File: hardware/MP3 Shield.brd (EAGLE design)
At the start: 53.3 x 59.7 mm, 62 parts, among them J1 ISP/SPI, Q1 12.288MHz, U1 3.3V, U2 ARDUINO_R3_SHIELD, U3 VS1053, U4 1.8V, U6 USD-SOCKET, U7 74HC4050 LVL CONVERTER

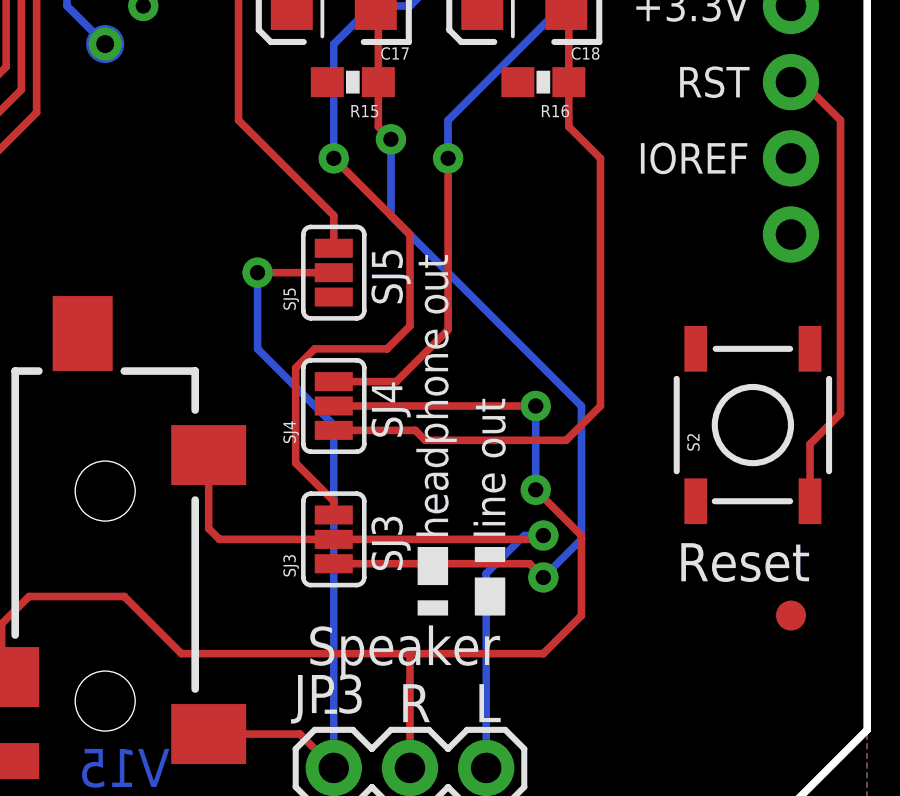
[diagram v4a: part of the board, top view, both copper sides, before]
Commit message: Tweaking after review
Clarifying solder jumpers for output configuration.
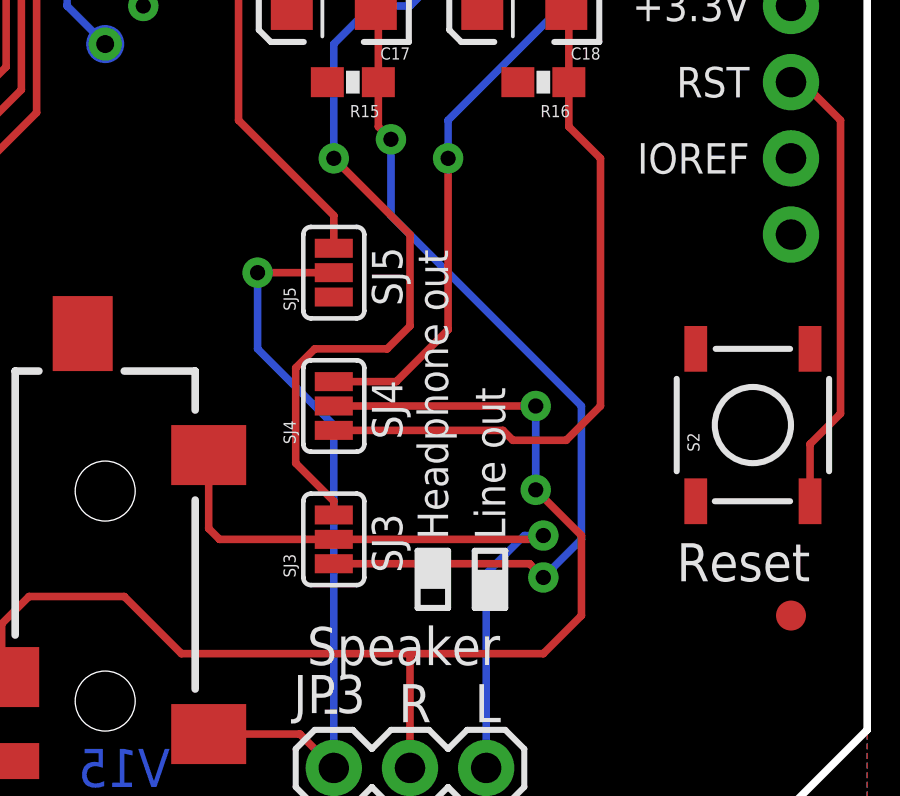
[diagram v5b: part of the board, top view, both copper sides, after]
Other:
- board text added: "Headphone out"
- board text added: "Line out"
- board text removed: "headphone out"
- board text removed: "line out"
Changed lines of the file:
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@@
 <text x="36.83" y="17.653" size="1.016" layer="21" font="vector" ratio="15" rot="R90" align="top-center">SJ5</text>
 <text x="11.43" y="-27.94" size="1.778" layer="51" font="vector" ratio="15">Byron Jacquot</text>
-<rectangle x1="38.354" y1="6.35" x2="39.37" y2="6.858" layer="21"/>
-<rectangle x1="40.259" y1="8.128" x2="41.275" y2="8.636" layer="21"/>
-<rectangle x1="38.354" y1="7.366" x2="39.37" y2="8.636" layer="21"/>
-<rectangle x1="40.259" y1="6.35" x2="41.275" y2="7.62" layer="21"/>
-<text x="38.354" y="8.89" size="1.016" layer="21" font="vector" ratio="15" rot="R90" align="top-left">headphone out</text>
-<text x="40.259" y="8.89" size="1.016" layer="21" font="vector" ratio="15" rot="R90" align="top-left">line out</text>
+<rectangle x1="38.354" y1="7.239" x2="39.37" y2="8.509" layer="21"/>
+<text x="38.354" y="8.89" size="1.016" layer="21" font="vector" ratio="15" rot="R90" align="top-left">Headphone out</text>
+<text x="40.259" y="8.89" size="1.016" layer="21" font="vector" ratio="15" rot="R90" align="top-left">Line out</text>
+<wire x1="38.354" y1="8.509" x2="38.354" y2="6.604" width="0.2032" layer="21"/>
+<wire x1="38.354" y1="6.604" x2="39.37" y2="6.604" width="0.2032" layer="21"/>
+<wire x1="39.37" y1="6.604" x2="39.37" y2="8.509" width="0.2032" layer="21"/>
+<wire x1="39.37" y1="8.509" x2="38.354" y2="8.509" width="0.2032" layer="21"/>
+<rectangle x1="40.259" y1="6.604" x2="41.275" y2="7.874" layer="21" rot="R180"/>
+<wire x1="41.275" y1="6.604" x2="41.275" y2="8.509" width="0.2032" layer="21"/>
+<wire x1="41.275" y1="8.509" x2="40.259" y2="8.509" width="0.2032" layer="21"/>
+<wire x1="40.259" y1="8.509" x2="40.259" y2="6.604" width="0.2032" layer="21"/>
+<wire x1="40.259" y1="6.604" x2="41.275" y2="6.604" width="0.2032" layer="21"/>
 </plain>
 <attributes>
@@
 <wire x1="44.45" y1="13.335" x2="44.45" y2="21.59" width="0.254" layer="1"/>
 <wire x1="43.307" y1="12.192" x2="44.45" y2="13.335" width="0.254" layer="1"/>
-<wire x1="35.56" y1="12.5222" x2="38.2778" y2="12.5222" width="0.254" layer="1"/>
-<wire x1="38.2778" y1="12.5222" x2="38.608" y2="12.192" width="0.254" layer="1"/>
-<wire x1="38.608" y1="12.192" x2="43.307" y2="12.192" width="0.254" layer="1"/>
+<wire x1="35.56" y1="12.5222" x2="41.1988" y2="12.5222" width="0.254" layer="1"/>
+<wire x1="41.1988" y1="12.5222" x2="41.529" y2="12.192" width="0.254" layer="1"/>
+<wire x1="41.529" y1="12.192" x2="43.307" y2="12.192" width="0.254" layer="1"/>
 <wire x1="43.395" y1="24.13" x2="43.395" y2="22.645" width="0.254" layer="1"/>
 <wire x1="43.395" y1="22.645" x2="44.45" y2="21.59" width="0.254" layer="1"/>
